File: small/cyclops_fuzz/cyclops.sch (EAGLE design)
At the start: 44 parts, among them IC1 4558, IC2 741

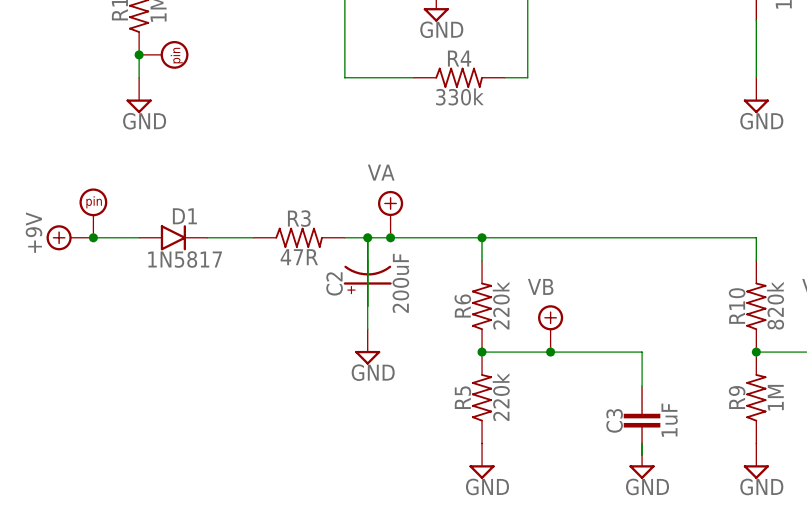
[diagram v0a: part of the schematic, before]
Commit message: add EAGLE library, update 1590a chorus and tremolo, other minor edits
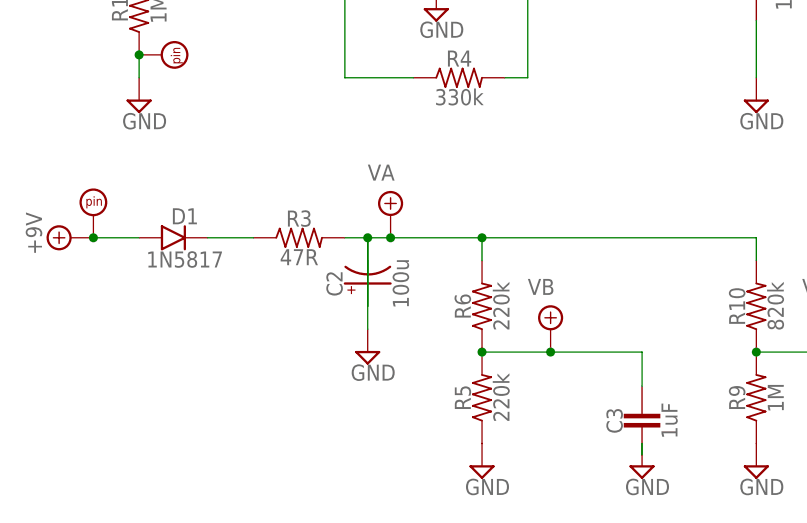
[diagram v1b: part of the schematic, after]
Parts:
- C2: value 200uF -> 100u
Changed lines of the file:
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@@
 <part name="C1" library="capacitors-film" deviceset="CER/FILM" device="BOX.1" value="150nF"/>
 <part name="R2" library="resistors" deviceset="R_" device=".2" value="56k"/>
-<part name="C2" library="capacitors-elec" deviceset="063" device="1" value="200uF"/>
+<part name="C2" library="capacitors-elec" deviceset="063" device="1" value="100u"/>
 <part name="R6" library="resistors" deviceset="R_" device=".2" value="220k"/>
 <part name="R5" library="resistors" deviceset="R_" device=".2" value="220k"/>
